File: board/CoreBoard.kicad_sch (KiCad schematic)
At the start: 0 parts

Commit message: Finished the teensy pins I think
Imported decoder and set up pins for it, also I made a general layout
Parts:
- added C1: 10µF, Capacitor_SMD:C_1206_3216Metric_Pad1.33x1.80mm_HandSolder, symbol Device:C
- added C2: 10µF, Capacitor_SMD:C_0603_1608Metric_Pad1.08x0.95mm_HandSolder, symbol Device:C
- added C3: 0.1µF, Capacitor_SMD:C_0603_1608Metric_Pad1.08x0.95mm_HandSolder, symbol Device:C
- added Conn1: AndersonPP, MRDT_Connectors:Square_Anderson_2_H_Side_By_Side_PV, symbol MRDT_Connectors:AndersonPP
- added Conn2: Molex_SL_03, MRDT_Connectors:MOLEX_SL_03_Vertical, symbol MRDT_Connectors:Molex_SL_03
- added Conn3, Conn4, Conn5, Conn6, Conn7: Molex_SL_09, MRDT_Connectors:MOLEX_SL_09_Horizontal, symbol MRDT_Connectors:Molex_SL_09
- added D1, D2, D3: Green, LED_SMD:LED_0603_1608Metric_Pad1.05x0.95mm_HandSolder, symbol Device:LED
- added D10, D11, D7, D9: Blue, LED_SMD:LED_0603_1608Metric_Pad1.05x0.95mm_HandSolder, symbol Device:LED
- added H1, H2, H3, H4: MountingHole, MRDT_Drill_Holes:4_40_Hole, symbol Mechanical:MountingHole
- added J1: RJ45_LED_Shielded, MRDT_Connectors:RJ45_Teensy, symbol Connector:RJ45_LED_Shielded
- added R1: 1.5k, Resistor_SMD:R_0603_1608Metric_Pad0.98x0.95mm_HandSolder, symbol Device:R
- added R10, R14, R16, R18: 4.7k, Resistor_SMD:R_0603_1608Metric_Pad0.98x0.95mm_HandSolder, symbol Device:R
- added R11, R15, R17, R19, R2: 100, Resistor_SMD:R_0603_1608Metric_Pad0.98x0.95mm_HandSolder, symbol Device:R
- added R3: 220, Resistor_SMD:R_0603_1608Metric_Pad0.98x0.95mm_HandSolder, symbol Device:R
- added SW11, SW12, SW13, SW14, SW15, SW16, SW17: SW_Wuerth_450301014042, MRDT_Switches:SW_Switch_03_STSSS9121_Through_Hole, symbol Switch:SW_Wuerth_450301014042
- added SW4, SW6, SW7, SW8: SW_Push, Button_Switch_SMD:SW_SPST_TL3305A, symbol Switch:SW_Push
- added U1: 74VHC138FT, TSSOP16B_TOS, symbol CoreBoard:74VHC138FT
- added U2: OKI, MRDT_Devices:OKI_Horizontal, symbol MRDT_Devices:OKI
- added U2: Teensy4.1_DEV-16771, MRDT_Shields:Teensy_4_1_Ethernet, symbol MRDT_Shields:Teensy4.1_DEV-16771
- added U3: SHHD003A0A, MRDT_Devices:SHHD003A0A41Z_Through_Hole, symbol MRDT_Devices:SHHD003A0A
- added U4: GY-521, GY-521:GY-521, symbol GY-521:GY-521
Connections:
- new net: D11.1 (K), R19.1
- new net: D9.1 (K), R15.1
- new net: D10.1 (K), R17.1
- new net: C3.1, J1.2, J1.5
- new net: D7.1 (K), R11.1
- new net: D1.2 (A), R1.2
- new net: D2.2 (A), R2.2
- new net: D3.2 (A), R3.2
- new net +3.3V: D10.2 (A), D11.2 (A), D7.2 (A), D9.2 (A), R10.1, R14.1, R16.1, R18.1, R2.1, SW11.3 (A), SW12.3 (A), SW13.3 (A), SW14.3 (A), SW15.3 (A), SW16.3 (A), SW17.3 (A), U1.16 (VCC), U1.6 (G1), U2.3.3V_1 (3.3V), U2.3.3V_2 (3.3V), U2.3.3V_3 (3.3V)
- new net +5V: C2.1, Conn5.2, Conn5.5, Conn5.8, Conn6.2, Conn6.5, Conn6.8, Conn7.2, Conn7.5, Conn7.8, R3.1, U2.3 (Vo), U2.VIN, U4.VCC
- new net 5V: Conn2.1, U3.6 (Vout+)
- new net AccSCL: U2.19 (A5), U4.SCL
- new net AccSDA: U2.18 (A4), U4.SDA
- new net B0: U2.32 (OUT1B)
- new net B1: U2.13 (SCK)
- new net B2: R18.2, R19.2, SW8.2, U2.27 (A13)
- new net B3: U2.22 (A8)
- new net B4: R14.2, R15.2, SW6.2
- new net B6: R16.2, R17.2, SW7.2
- new net B8: R10.2, R11.2, SW4.2
- new net BL_RX: Conn3.2, U2.34 (RX8)
- new net BL_TX: Conn3.1, U2.35 (TX8)
- new net BR_RX: Conn4.8, U2.21 (A7)
- new net BR_TX: Conn4.9, U2.20 (A6)
- new net DS1: SW11.1 (B)
- new net DS2: SW12.1 (B)
- new net DS3: SW13.1 (B)
- new net DS4: SW14.1 (B)
- new net DS5: SW15.1 (B)
- new net DS6: SW16.1 (B)
- new net DS7: SW17.1 (B)
- new net FL_RX: Conn3.8, U2.0 (RX1)
- new net FL_TX: Conn3.7, U2.1 (TX1)
- new net FPWM0: U2.9 (OUT1C)
- new net FPWM1: U2.4 (BCLK2)
- new net FPWM2: U2.3 (LRCLK2)
- new net FPWM3: U2.33 (MCLK2)
- new net FR_RX: Conn4.2, U2.15 (A1)
- new net FR_TX: Conn4.3, U2.14 (A0)
- new net GND: C1.2, C2.2, C3.2, Conn1.1 (GND), Conn2.2, Conn3.3, Conn3.6, Conn3.9, Conn4.1, Conn4.4, Conn4.7, Conn5.1, Conn5.4, Conn5.7, Conn6.1, Conn6.4, Conn6.7, Conn7.1, Conn7.4, Conn7.7, D1.1 (K), D2.1 (K), D3.1 (K), J1.8, J1.9, J1.SH, SW11.2 (C), SW12.2 (C), SW13.2 (C), SW14.2 (C), SW15.2 (C), SW16.2 (C), SW17.2 (C), SW4.1, SW6.1, SW7.1, SW8.1, U1.4 (*G2A), U1.5 (*G2B), U1.8 (GND), U2.2 (GND), U2.GND1 (GND), U2.GND2 (GND), U2.GND3 (GND), U2.GND4 (GND), U2.GND5 (GND), U2.USB_GND1 (USB_GND), U2.USB_GND2 (USB_GND), U3.2 (Vin-), U3.3 (On/OFF), U3.4 (Vout-), U4.ADO, U4.GND
- new net LED: J1.10, U2.LED
- new net ML_RX: Conn3.5, U2.28 (RX7)
- new net ML_TX: Conn3.4, U2.29 (TX7)
- new net MR_RX: Conn4.5, U2.16 (A2)
- new net MR_TX: Conn4.6, U2.17 (A3)
- new net NeoPixels: Conn2.3
- new net RB0: U1.1 (A), U2.26 (A12)
- new net RB1: U1.2 (B), U2.30 (CRX3)
- new net RB2: U1.3 (C), U2.31 (CTX3)
- new net Rx+: J1.4, U2.R+
- new net Rx-: J1.6, U2.R-
- new net ServoPWM1: Conn5.9, U2.7 (RX2)
- new net ServoPWM2: Conn5.6, U2.8 (TX2)
- new net ServoPWM3: Conn5.3, U2.2 (OUT2)
- new net ServoPWM4: Conn6.9, U2.11 (MOSI)
- new net ServoPWM5: Conn6.6, U2.6 (OUT1D)
- new net ServoPWM6: Conn6.3, U2.12 (MISO)
- new net ServoPWM7: Conn7.9, U2.5 (IN2)
- new net ServoPWM8: Conn7.6, U2.10 (CS1)
- new net ServoPWM9: Conn7.3
- new net TS0: U2.24 (A10)
- new net TS1: U2.25 (A11)
- new net Tx+: J1.1, U2.T+
- new net Tx-: J1.3, U2.T-
- new net VCC: C1.1, Conn1.4 (PV+), R1.1, U2.1 (Vi), U3.1 (Vin+)
- new net WS0: U2.38 (A14)
- new net WS1: U2.39 (A15)
- new net WS2: U2.40 (A16)
- new net WS3: U2.41 (A17)
- new net WS4: U2.36 (CS2)
- new net WS5: U2.37 (CS3)
- no-connect marks 0 -> 14
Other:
- note added: "Accelerometer"
- note added: "Decoder"
- note added: "Gimbal Buttons"
- note added: "Holes"
- note added: "LED System"
- note added: "Motor Switches & Rotary Encoder"
- note added: "NeoPixels"
- note added: "Power"
- note added: "Power LED"
- note added: "Servo Communication"
- note added: "Teensy"
- note added: "VESC Serial"
- note added: "Y7"

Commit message: Converted schematic to hierarchical sheets
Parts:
- removed C1: 10µF, Capacitor_SMD:C_1206_3216Metric_Pad1.33x1.80mm_HandSolder, symbol Device:C
- removed C2: 10µF, Capacitor_SMD:C_0603_1608Metric_Pad1.08x0.95mm_HandSolder, symbol Device:C
- removed C3: 0.1µF, Capacitor_SMD:C_0603_1608Metric_Pad1.08x0.95mm_HandSolder, symbol Device:C
- removed Conn1: AndersonPP, MRDT_Connectors:Square_Anderson_2_H_Side_By_Side_PV, symbol MRDT_Connectors:AndersonPP
- removed Conn2: Molex_SL_03, MRDT_Connectors:MOLEX_SL_03_Vertical, symbol MRDT_Connectors:Molex_SL_03
- removed Conn3, Conn4, Conn5, Conn6, Conn7: Molex_SL_09, MRDT_Connectors:MOLEX_SL_09_Horizontal, symbol MRDT_Connectors:Molex_SL_09
- removed D1, D2, D3: Green, LED_SMD:LED_0603_1608Metric_Pad1.05x0.95mm_HandSolder, symbol Device:LED
- removed D10, D11, D7, D9: Blue, LED_SMD:LED_0603_1608Metric_Pad1.05x0.95mm_HandSolder, symbol Device:LED
- removed J1: RJ45_LED_Shielded, MRDT_Connectors:RJ45_Teensy, symbol Connector:RJ45_LED_Shielded
- removed R1: 1.5k, Resistor_SMD:R_0603_1608Metric_Pad0.98x0.95mm_HandSolder, symbol Device:R
- removed R10, R14, R16, R18: 4.7k, Resistor_SMD:R_0603_1608Metric_Pad0.98x0.95mm_HandSolder, symbol Device:R
- removed R11, R15, R17, R19, R2: 100, Resistor_SMD:R_0603_1608Metric_Pad0.98x0.95mm_HandSolder, symbol Device:R
- removed R3: 220, Resistor_SMD:R_0603_1608Metric_Pad0.98x0.95mm_HandSolder, symbol Device:R
- removed SW11, SW12, SW13, SW14, SW15, SW16, SW17: SW_Wuerth_450301014042, MRDT_Switches:SW_Switch_03_STSSS9121_Through_Hole, symbol Switch:SW_Wuerth_450301014042
- removed SW4, SW6, SW7, SW8: SW_Push, Button_Switch_SMD:SW_SPST_TL3305A, symbol Switch:SW_Push
- removed U1: 74VHC138FT, TSSOP16B_TOS, symbol CoreBoard:74VHC138FT
- removed U2: OKI, MRDT_Devices:OKI_Horizontal, symbol MRDT_Devices:OKI
- removed U2: Teensy4.1_DEV-16771, MRDT_Shields:Teensy_4_1_Ethernet, symbol MRDT_Shields:Teensy4.1_DEV-16771
- removed U3: SHHD003A0A, MRDT_Devices:SHHD003A0A41Z_Through_Hole, symbol MRDT_Devices:SHHD003A0A
- removed U4: GY-521, GY-521:GY-521, symbol GY-521:GY-521
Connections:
- no-connect marks 14 -> 0
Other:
- added sheet Accelerometer (accelerometer.kicad_sch)
- added sheet Gimbal Servos (gimbals.kicad_sch)
- added sheet Lighting (lighting.kicad_sch)
- added sheet Motor VESCs (drive.kicad_sch)
- added sheet Power (power.kicad_sch)
- added sheet Selection LEDs (led_decoder.kicad_sch)
- added sheet Teensy (teensy.kicad_sch)
- added sheet Test Buttons (test_buttons.kicad_sch)
- note removed: "Accelerometer"
- note removed: "Decoder"
- note removed: "Gimbal Buttons"
- note removed: "LED System"
- note removed: "Motor Switches & Rotary Encoder"
- note removed: "NeoPixels"
- note removed: "Power"
- note removed: "Power LED"
- note removed: "Servo Communication"
- note removed: "Teensy"
- note removed: "VESC Serial"
- note removed: "Y7"

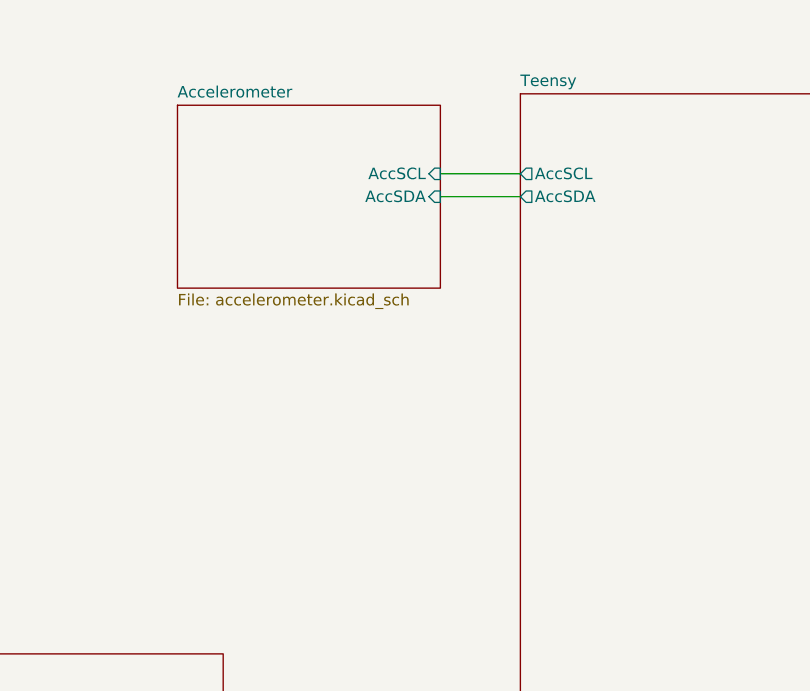
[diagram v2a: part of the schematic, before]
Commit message: Added Temp Sensor
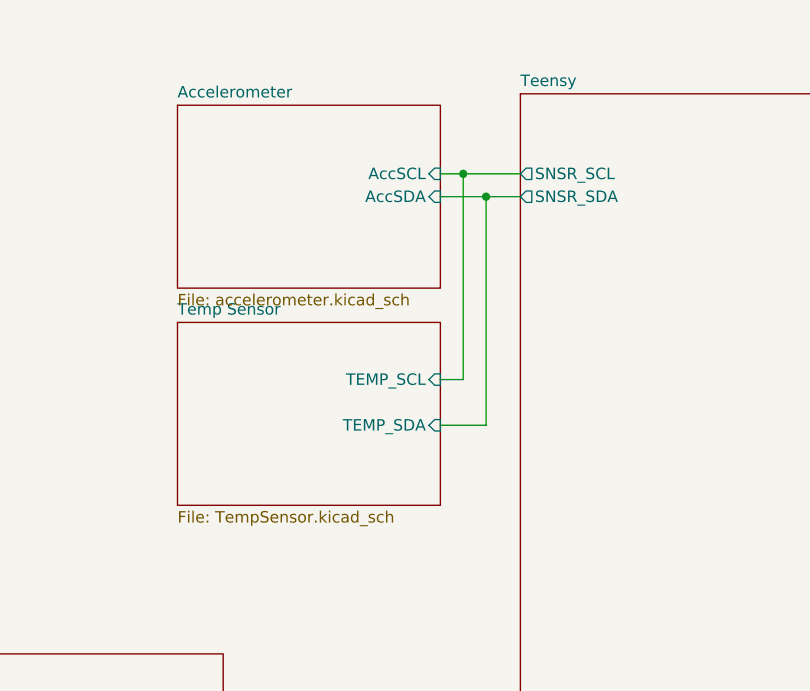
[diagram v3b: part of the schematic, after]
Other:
- added sheet Temp Sensor (TempSensor.kicad_sch)
- sheet Teensy ports: added SNSR_SCL, SNSR_SDA; removed AccSCL, AccSDA
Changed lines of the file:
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@@
+	)
+	(junction
+		(at 170.18 96.52)
+		(diameter 0)
+		(color 0 0 0 0)
+	)
+	(junction
+		(at 172.72 99.06)
+		(diameter 0)
+		(color 0 0 0 0)
 	)
 	(junction
@@
 	(wire
 		(pts
-			(xy 167.64 99.06) (xy 176.53 99.06)
+			(xy 167.64 99.06) (xy 172.72 99.06)
 		)
 		(stroke
@@
 	(wire
 		(pts
+			(xy 172.72 99.06) (xy 176.53 99.06)
+		)
+		(stroke
+			(width 0)
+			(type default)
+		)
+	)
+	(wire
+		(pts
 			(xy 233.68 139.7) (xy 246.38 139.7)
 		)
@@
 	(wire
 		(pts
+			(xy 172.72 124.46) (xy 172.72 99.06)
+		)
+		(stroke
+			(width 0)
+			(type default)
+		)
+	)
+	(wire
+		(pts
 			(xy 233.68 100.33) (xy 246.38 100.33)
 		)
@@
 	(wire
 		(pts
+			(xy 170.18 96.52) (xy 176.53 96.52)
+		)
+		(stroke
+			(width 0)
+			(type default)
+		)
+	)
+	(wire
+		(pts
 			(xy 143.51 175.26) (xy 153.67 175.26)
 		)
@@
 	(wire
 		(pts
+			(xy 167.64 119.38) (xy 170.18 119.38)
+		)
+		(stroke
+			(width 0)
+			(type default)
+		)
+	)
+	(wire
+		(pts
 			(xy 160.02 210.82) (xy 160.02 180.34)
 		)
@@
 	(wire
 		(pts
-			(xy 167.64 96.52) (xy 176.53 96.52)
+			(xy 167.64 96.52) (xy 170.18 96.52)
 		)
 		(stroke
@@
 	(wire
 		(pts
+			(xy 167.64 124.46) (xy 172.72 124.46)
+		)
+		(stroke
+			(width 0)
+			(type default)
+		)
+	)
+	(wire
+		(pts
 			(xy 148.59 170.18) (xy 148.59 210.82)
 		)
@@
 		(pts
 			(xy 233.68 142.24) (xy 246.38 142.24)
+		)
+		(stroke
+			(width 0)
+			(type default)
+		)
+	)
+	(wire
+		(pts
+			(xy 170.18 119.38) (xy 170.18 96.52)
 		)
 		(stroke
@@
 	)
 	(sheet
+		(at 138.43 113.03)
+		(size 29.21 20.32)
+		(exclude_from_sim no)
+		(in_bom yes)
+		(on_board yes)
+		(dnp no)
+		(fields_autoplaced yes)
+		(stroke
+			(width 0.1524)
+			(type solid)
+		)
+		(fill
+			(color 0 0 0 0.0000)
+		)
+		(property "Sheetname" "Temp Sensor"
+			(at 138.43 112.3184 0)
+			(effects
+				(font
+					(size 1.27 1.27)
+				)
+				(justify left bottom)
+			)
+		)
+		(property "Sheetfile" "TempSensor.kicad_sch"
+			(at 138.43 133.9346 0)
+			(effects
+				(font
+					(size 1.27 1.27)
+				)
+				(justify left top)
+			)
+		)
+		(pin "TEMP_SCL" input
+			(at 167.64 119.38 0)
+			(effects
+				(font
+					(size 1.27 1.27)
+				)
+				(justify right)
+			)
+		)
+		(pin "TEMP_SDA" input
+			(at 167.64 124.46 0)
+			(effects
+				(font
+					(size 1.27 1.27)
+				)
+				(justify right)
+			)
+		)
+		(instances
+			(project "CoreBoard"
+				(path "/044aaf9e-f771-40cc-9be3-702621321f68"
+					(page "10")
+				)
+			)
+		)
+	)
+	(sheet
 		(at 91.44 149.86)
 		(size 52.07 49.53)
@@
 			)
 		)
-		(pin "AccSCL" output
-			(at 176.53 96.52 180)
-			(effects
-				(font
-					(size 1.27 1.27)
-				)
-				(justify left)
-			)
-		)
-		(pin "AccSDA" output
-			(at 176.53 99.06 180)
-			(effects
-				(font
-					(size 1.27 1.27)
-				)
-				(justify left)
-			)
-		)
 		(pin "BackPan" output
 			(at 233.68 106.68 0)
@@
 			)
 		)
+		(pin "SNSR_SCL" output
+			(at 176.53 96.52 180)
+			(effects
+				(font
+					(size 1.27 1.27)
+				)
+				(justify left)
+			)
+		)
+		(pin "SNSR_SDA" output
+			(at 176.53 99.06 180)
+			(effects
+				(font
+					(size 1.27 1.27)
+				)
+				(justify left)
+			)
+		)

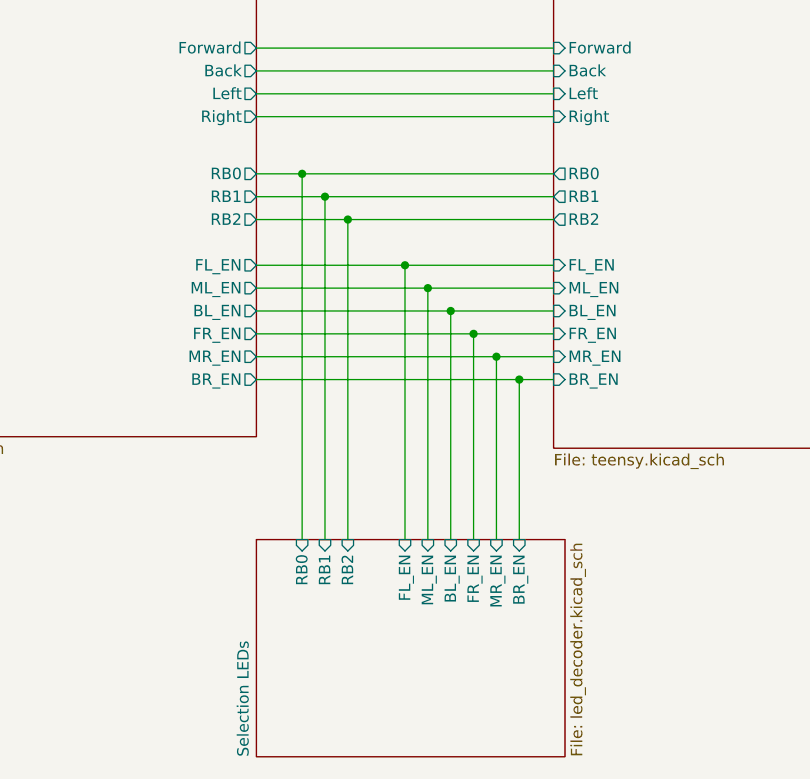
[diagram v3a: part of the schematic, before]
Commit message: Added Rotary Encoder
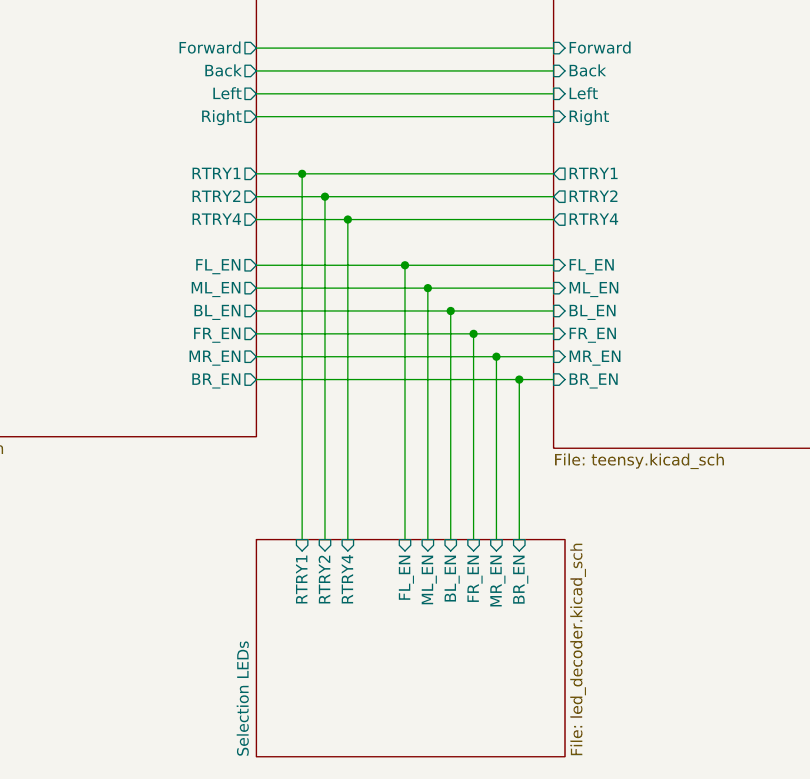
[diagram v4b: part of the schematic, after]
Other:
- sheet Selection LEDs ports: added RTRY1, RTRY2, RTRY4; removed RB0, RB1, RB2
- sheet Teensy ports: added RTRY1, RTRY2, RTRY4; removed RB0, RB1, RB2
- sheet Test Buttons ports: added RTRY1, RTRY2, RTRY4; removed RB0, RB1, RB2
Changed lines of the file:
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@@
-			)
-		)
-		(pin "RB0" input
-			(at 148.59 210.82 90)
-			(effects
-				(font
-					(size 1.27 1.27)
-				)
-				(justify right)
-			)
-		)
-		(pin "RB1" input
-			(at 151.13 210.82 90)
-			(effects
-				(font
-					(size 1.27 1.27)
-				)
-				(justify right)
-			)
-		)
-		(pin "RB2" input
-			(at 153.67 210.82 90)
-			(effects
-				(font
-					(size 1.27 1.27)
-				)
-				(justify right)
 			)
 		)
@@
 		(pin "FR_EN" input
 			(at 167.64 210.82 90)
+			(effects
+				(font
+					(size 1.27 1.27)
+				)
+				(justify right)
+			)
+		)
+		(pin "RTRY1" input
+			(at 148.59 210.82 90)
+			(effects
+				(font
+					(size 1.27 1.27)
+				)
+				(justify right)
+			)
+		)
+		(pin "RTRY2" input
+			(at 151.13 210.82 90)
+			(effects
+				(font
+					(size 1.27 1.27)
+				)
+				(justify right)
+			)
+		)
+		(pin "RTRY4" input
+			(at 153.67 210.82 90)
 			(effects
 				(font
@@
 			)
 		)
-		(pin "RB0" output
+		(pin "RTRY1" output
 			(at 143.51 170.18 0)
 			(effects
@@
 			)
 		)
-		(pin "RB1" output
+		(pin "RTRY2" output
 			(at 143.51 172.72 0)
 			(effects
@@
 			)
 		)
-		(pin "RB2" output
+		(pin "RTRY4" output
 			(at 143.51 175.26 0)
 			(effects
@@
 			)
 		)
-		(pin "RB0" output
+		(pin "RTRY1" output
 			(at 176.53 170.18 180)
 			(effects
@@
 			)
 		)
-		(pin "RB1" output
+		(pin "RTRY2" output
 			(at 176.53 172.72 180)
 			(effects
@@
 			)
 		)
-		(pin "RB2" output
+		(pin "RTRY4" output
 			(at 176.53 175.26 180)
 			(effects

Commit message: Fan, Light, Buck
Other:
- added sheet Fans (coreboard_fans.kicad_sch)
- sheet Teensy ports: added FPWM1, FPWM2, FTACH1, FTACH2; removed none
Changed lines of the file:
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@@
 	(wire
 		(pts
-			(xy 172.72 124.46) (xy 172.72 99.06)
+			(xy 172.72 119.38) (xy 172.72 99.06)
 		)
 		(stroke
@@
 	(wire
 		(pts
-			(xy 167.64 119.38) (xy 170.18 119.38)
+			(xy 167.64 114.3) (xy 170.18 114.3)
+		)
+		(stroke
+			(width 0)
+			(type default)
+		)
+	)
+	(wire
+		(pts
+			(xy 167.64 140.97) (xy 176.53 140.97)
 		)
 		(stroke
@@
 	(wire
 		(pts
+			(xy 167.64 143.51) (xy 176.53 143.51)
+		)
+		(stroke
+			(width 0)
+			(type default)
+		)
+	)
+	(wire
+		(pts
 			(xy 143.51 156.21) (xy 176.53 156.21)
 		)
@@
 	(wire
 		(pts
+			(xy 167.64 137.16) (xy 176.53 137.16)
+		)
+		(stroke
+			(width 0)
+			(type default)
+		)
+	)
+	(wire
+		(pts
 			(xy 167.64 96.52) (xy 170.18 96.52)
 		)
@@
 	(wire
 		(pts
-			(xy 167.64 124.46) (xy 172.72 124.46)
+			(xy 167.64 119.38) (xy 172.72 119.38)
 		)
 		(stroke
@@
 	(wire
 		(pts
+			(xy 167.64 134.62) (xy 176.53 134.62)
+		)
+		(stroke
+			(width 0)
+			(type default)
+		)
+	)
+	(wire
+		(pts
 			(xy 233.68 142.24) (xy 246.38 142.24)
 		)
@@
 	(wire
 		(pts
-			(xy 170.18 119.38) (xy 170.18 96.52)
+			(xy 170.18 114.3) (xy 170.18 96.52)
 		)
 		(stroke
@@
 	)
 	(sheet
-		(at 138.43 88.9)
-		(size 29.21 20.32)
+		(at 146.05 88.9)
+		(size 21.59 13.97)
 		(exclude_from_sim no)
 		(in_bom yes)
@@
 		)
 		(property "Sheetname" "Accelerometer"
-			(at 138.43 88.1884 0)
+			(at 146.05 88.1884 0)
 			(effects
 				(font
@@
 		)
 		(property "Sheetfile" "accelerometer.kicad_sch"
-			(at 138.43 109.8046 0)
+			(at 146.05 103.4546 0)
 			(effects
 				(font
@@
 	)
 	(sheet
-		(at 138.43 113.03)
-		(size 29.21 20.32)
+		(at 146.05 132.08)
+		(size 21.59 15.24)
 		(exclude_from_sim no)
 		(in_bom yes)
@@
 			(color 0 0 0 0.0000)
 		)
+		(property "Sheetname" "Fans"
+			(at 146.05 131.3684 0)
+			(effects
+				(font
+					(size 1.27 1.27)
+				)
+				(justify left bottom)
+			)
+		)
+		(property "Sheetfile" "coreboard_fans.kicad_sch"
+			(at 146.05 147.9046 0)
+			(effects
+				(font
+					(size 1.27 1.27)
+				)
+				(justify left top)
+			)
+		)
+		(pin "PWM1" input
+			(at 167.64 137.16 0)
+			(effects
+				(font
+					(size 1.27 1.27)
+				)
+				(justify right)
+			)
+		)
+		(pin "PWM2" input
+			(at 167.64 143.51 0)
+			(effects
+				(font
+					(size 1.27 1.27)
+				)
+				(justify right)
+			)
+		)
+		(pin "Tach1" output
+			(at 167.64 134.62 0)
+			(effects
+				(font
+					(size 1.27 1.27)
+				)
+				(justify right)
+			)
+		)
+		(pin "Tach2" output
+			(at 167.64 140.97 0)
+			(effects
+				(font
+					(size 1.27 1.27)
+				)
+				(justify right)
+			)
+		)
+		(instances
+			(project "CoreBoard"
+				(path "/044aaf9e-f771-40cc-9be3-702621321f68"
+					(page "11")
+				)
+			)
+		)
+	)
+	(sheet
+		(at 146.05 107.95)
+		(size 21.59 13.97)
+		(exclude_from_sim no)
+		(in_bom yes)
+		(on_board yes)
+		(dnp no)
+		(fields_autoplaced yes)
+		(stroke
+			(width 0.1524)
+			(type solid)
+		)
+		(fill
+			(color 0 0 0 0.0000)
+		)
 		(property "Sheetname" "Temp Sensor"
-			(at 138.43 112.3184 0)
+			(at 146.05 107.2384 0)
 			(effects
 				(font
@@
 		)
 		(property "Sheetfile" "TempSensor.kicad_sch"
-			(at 138.43 133.9346 0)
+			(at 146.05 122.5046 0)
 			(effects
 				(font
@@
 		)
 		(pin "TEMP_SCL" input
+			(at 167.64 114.3 0)
+			(effects
+				(font
+					(size 1.27 1.27)
+				)
+				(justify right)
+			)
+		)
+		(pin "TEMP_SDA" input
 			(at 167.64 119.38 0)
-			(effects
-				(font
-					(size 1.27 1.27)
-				)
-				(justify right)
-			)
-		)
-		(pin "TEMP_SDA" input
-			(at 167.64 124.46 0)
 			(effects
 				(font
@@
 			(effects
 				(font
+					(size 1.27 1.27)
+				)
+				(justify left)
+			)
+		)
+		(pin "FPWM1" output
+			(at 176.53 137.16 180)
+			(effects
+				(font
+					(size 1.27 1.27)
+				)
+				(justify left)
+			)
+		)
+		(pin "FPWM2" output
+			(at 176.53 143.51 180)
+			(effects
+				(font
+					(size 1.27 1.27)
+				)
+				(justify left)
+			)
+		)
+		(pin "FTACH1" input
+			(at 176.53 134.62 180)
+			(effects
+				(font
+					(size 1.27 1.27)
+				)
+				(justify left)
+			)
+		)
+		(pin "FTACH2" input
+			(at 176.53 140.97 180)
+			(effects
+				(font
